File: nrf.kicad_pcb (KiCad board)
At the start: 2 copper layers, 24 parts, among them SW1 SW_DPST_x2, U1 BLYST-NRF52832-NANO, U2 Oled_128x64_SSD1306, U3 ECH8693R-TL-W, U4 C0720B001F, U5 MCP73871-xxI_ML, U6 LIS3DH

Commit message: More power setup
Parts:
- removed 100uF1, 10uF1: C_Small, Capacitors_SMD:C_0805
- added C4: 100nF, Capacitors_SMD:C_0805, F.Cu at (104.0, 73.0)
- added C5: 10uF, Capacitors_SMD:C_0805, F.Cu at (103.7, 78.2)
- added C6: 470pF, Capacitors_SMD:C_0805, F.Cu at (132.9, 96.0)
- added C7: 0.1uF, Capacitors_SMD:C_0805, F.Cu at (132.8, 100.2)
- added C8: 4.7uF, Capacitors_SMD:C_0805, F.Cu at (138.2, 97.7)
- added R11: 10K, Resistors_SMD:R_0805, F.Cu at (113.9, 61.2)
- added R12: 10K, Resistors_SMD:R_0805, F.Cu at (121.5, 61.4)
- added SW2: MID, my-fp-library:Tact_SW_3x6x3.5, F.Cu at (147.4, 59.8)
- added SW3: DWN, my-fp-library:Tact_SW_3x6x3.5, F.Cu at (157.6, 59.7)
- added U7: MIC5219-3.3BM5, TO_SOT_Packages_SMD:SOT-23-5, F.Cu at (138.3, 103.3)
- SW1: value SW_DPST_x2 -> UP; footprint Buttons_Switches_SMD:SW_DIP_x2_W5.08mm_Slide_Copal_CHS-A -> my-fp-library:Tact_SW_3x6x3.5
- moved SW1 37.8 mm to (137.2, 60.0)
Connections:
- net VBAT renamed /pwr/VBAT
- U1 pad 1: (no net) -> I2C_SDA
- U1 pad 11: (no net) -> /BTN_3
- U1 pad 13: (no net) -> /BTN_2
- U1 pad 2: (no net) -> I2C_SCL
- U6 pad 4: (no net) -> I2C_SCL
- U6 pad 6: (no net) -> I2C_SDA
- U6 pad 8: (no net) -> +3.3

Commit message: Connectors
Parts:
- added J1: Conn_01x02, my-fp-library:Battery Pads 3x3, F.Cu at (147.8, 112.7)
- added J2: Conn_01x05, Pin_Headers:Pin_Header_Straight_1x05_Pitch1.27mm, F.Cu at (142.7, 119.5)
- moved U1 35.1 mm to (117.0, 119.8), turned to 90 degrees
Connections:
- R1 pad 2: GND -> (GND)
- SW1 pad 1: GND -> (GND)
- SW2 pad 1: GND -> (GND)
- SW3 pad 1: GND -> (GND)
- U1 pad 18: (no net) -> /SWDIO
- U1 pad 19: (no net) -> /SWDCLK
- U1 pad 2: I2C_SCL -> /RESET
- U1 pad 3: (no net) -> I2C_SCL
- U2 pad 1: GND -> (GND)
- U2 pad 10: GND -> (GND)
- U2 pad 11: GND -> (GND)
- U2 pad 12: GND -> (GND)
- U2 pad 21: GND -> (GND)
- U2 pad 22: GND -> (GND)
- U2 pad 23: GND -> (GND)
- U2 pad 24: GND -> (GND)
- U2 pad 25: GND -> (GND)
- U2 pad 29: GND -> (GND)
- U2 pad 30: GND -> (GND)
- U2 pad 6: VDD -> +3.3
- U2 pad 8: GND -> (GND)
- U2 pad 9: VDD -> +3.3
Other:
- board outline added: 26.6 x 19.3 mm

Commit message: Layout power
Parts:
- moved R7 71.8 mm to (79.8, 77.0), turned to 180 degrees
- moved R6 70.4 mm to (79.8, 79.1)
- moved J1 70.4 mm to (77.7, 106.6)
- moved U5 68.0 mm to (84.2, 80.0)
- moved R4 67.7 mm to (75.2, 94.5)
- moved R8 67.2 mm to (88.8, 82.3)
- moved R10 65.6 mm to (79.8, 81.1), turned to 180 degrees
- moved R9 62.7 mm to (88.8, 80.2)
- moved R5 62.5 mm to (75.1, 89.9)
- moved D2 60.6 mm to (75.4, 87.8)
- moved C4 56.2 mm to (159.3, 82.8)
- moved R11 56.2 mm to (169.2, 70.9)
- moved R12 56.2 mm to (176.9, 71.1)
- moved U6 56.2 mm to (172.8, 83.3)
- moved C5 56.2 mm to (159.1, 87.9)
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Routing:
- net VBUS: track 0.00 -> 8.98 mm, vias 0 -> 3
- net Net-(C3-Pad1): track 0.00 -> 3.80 mm
- net Net-(R6-Pad2): track 0.00 -> 3.62 mm
- net Net-(R8-Pad1): track 0.00 -> 2.70 mm
- net (GND): track 0.00 -> 2.31 mm, vias 0 -> 6
- net Net-(R9-Pad1): track 0.00 -> 1.74 mm
- net Net-(R10-Pad1): track 0.00 -> 1.45 mm
- added copper zone on Gnd.Cu, net (GND)
- added copper zone on Pwr.Cu, net VBUS
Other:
- copper layers 2 -> 4

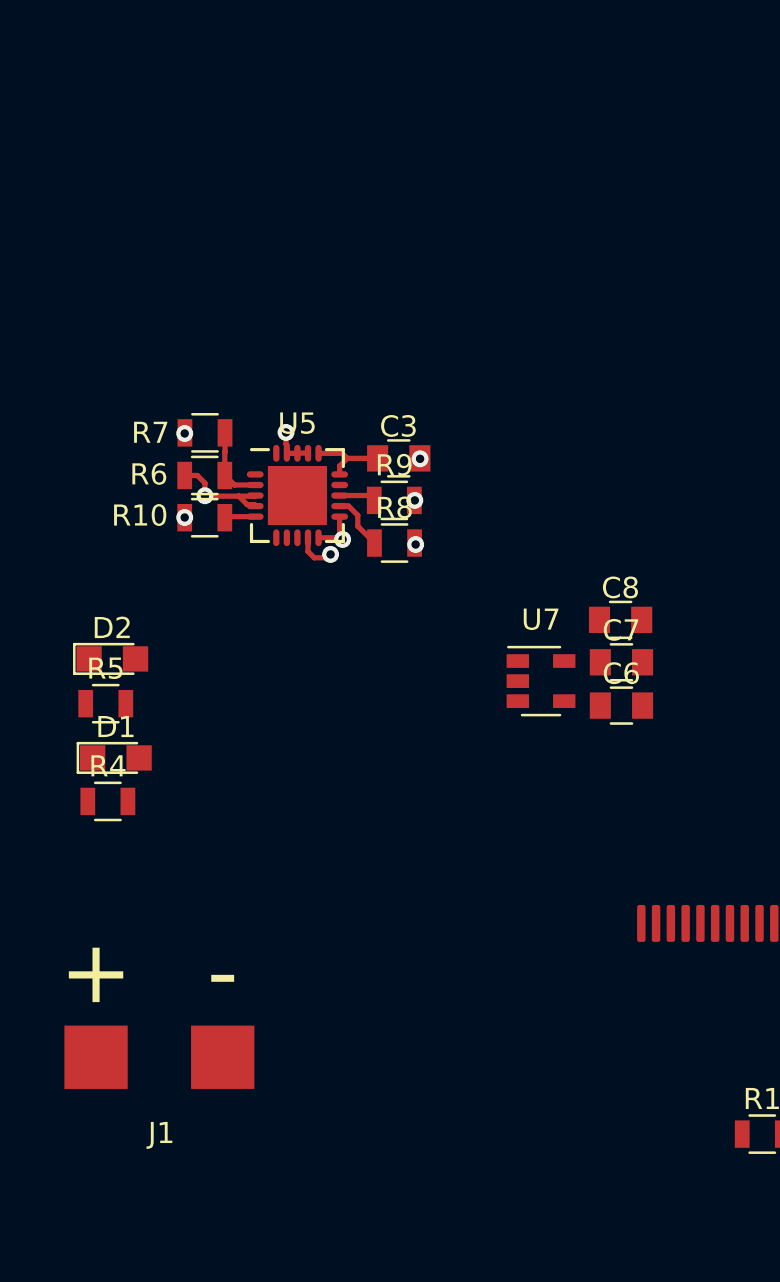
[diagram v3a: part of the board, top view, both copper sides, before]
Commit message: More power connections
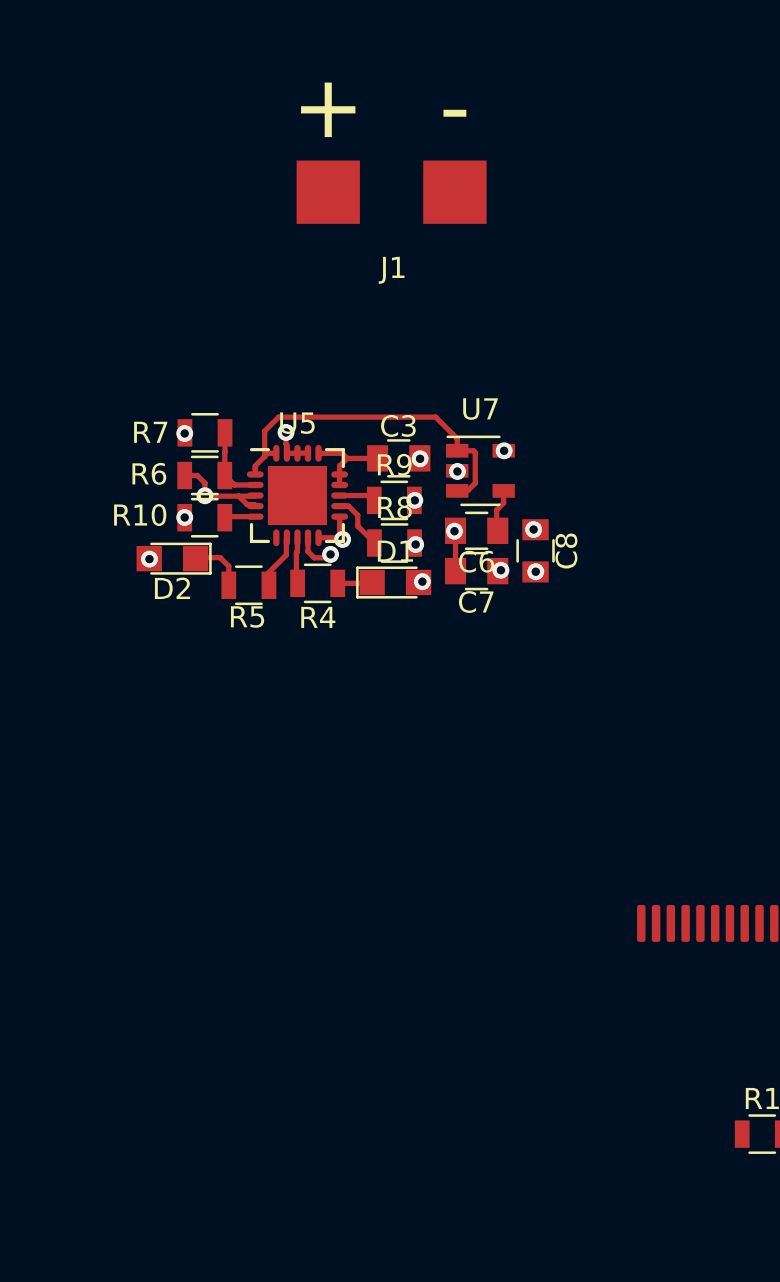
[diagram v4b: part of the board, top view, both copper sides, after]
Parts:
- moved J1 42.4 mm to (88.7, 65.6)
- moved D1 15.6 mm to (88.8, 84.1)
- moved R4 14.3 mm to (85.2, 84.2), turned to 180 degrees
- moved C6 10.8 mm to (92.7, 81.7), turned to 180 degrees
- moved U7 10.4 mm to (92.9, 78.8)
- moved R5 8.80 mm to (81.9, 84.3)
- moved C7 8.11 mm to (92.7, 83.6), turned to 180 degrees
- moved D2 5.54 mm to (78.3, 83.0), turned to 180 degrees
- moved C8 5.19 mm to (95.5, 82.6), turned to 270 degrees
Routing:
- net /pwr/VBAT: track 0.00 -> 16.6 mm
- net STAT: track 0.00 -> 2.61 mm
- net Net-(D2-Pad1): track 0.00 -> 2.60 mm
- net PWR_SENSE: track 0.00 -> 2.15 mm
- net Net-(C6-Pad1): track 0.00 -> 1.94 mm
- net (GND): track 2.31 -> 4.22 mm, vias 6 -> 9
- net Net-(D1-Pad1): track 0.00 -> 1.62 mm
- net VBUS: vias 3 -> 5
- net +3.3: vias 0 -> 3
- added copper zone on Pwr.Cu, net +3.3

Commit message: More PCB setup
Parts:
- Ue: renamed from U2; moved to B.Cu
- moved U1 88.3 mm to (81.3, 89.4)
- moved R12 77.5 mm to (100.1, 81.6)
- moved U6 72.4 mm to (100.6, 78.7)
- moved R11 66.1 mm to (103.5, 78.2), turned to 270 degrees
- moved C4 63.6 mm to (95.8, 78.8), turned to 90 degrees
- moved C5 61.9 mm to (97.6, 80.8), turned to 90 degrees
- moved J2 49.4 mm to (99.0, 96.5), turned to 90 degrees
- moved C1 39.7 mm to (89.5, 86.5)
- moved C2 39.0 mm to (88.6, 92.8)
- moved U4 27.9 mm to (99.1, 90.3), turned to 180 degrees
- moved Ue 21.4 mm to (91.9, 89.3)
- moved R1 19.2 mm to (100.8, 91.8)
- moved U3 13.0 mm to (103.8, 84.3)
- moved R3 12.0 mm to (103.8, 81.5)
- moved R2 9.02 mm to (100.3, 83.8)
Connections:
- R2 pad 1: GND -> (GND)
- U3 pad 1: GND -> (GND)
- U3 pad 3: GND -> (GND)
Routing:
- net +3.3: track 0.00 -> 13.7 mm, vias 3 -> 4
- net (GND): track 4.22 -> 12.2 mm, vias 9 -> 12
- net Net-(R3-Pad1): track 0.00 -> 3.37 mm
- net MOTOR_PWM: track 0.00 -> 2.46 mm
- net I2C_SCL: track 0.00 -> 1.64 mm
- net I2C_SDA: track 0.00 -> 1.60 mm
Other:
- net class Default: clearance 0.2 -> 0.1524; trace_width 0.25 -> 0.1524; via_dia 0.8 -> 0.6858; via_drill 0.4 -> 0.3302
- rule pad_to_mask_clearance: 0.051 -> 0.0508
- rule trace_clearance: 0.2 -> 0.1524
- rule trace_min: 0.2 -> 0.1524
- rule via_min_drill: 0.3 -> 0.254
- rule via_min_size: 0.4 -> 0.508

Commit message: Initial
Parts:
- removed J1: Conn_01x02, my-fp-library:Battery Pads 3x3
- removed U1: BLYST-NRF52832-NANO, my-fp-library:BLYST NRF52832-NANO
- removed U3: ECH8693R-TL-W, my-fp-library:SOT-28FL
- removed U4: C0720B001F, my-fp-library:VIBRATION MOTOR COIN 3V FLEX - C0720B001F
- removed U6: LIS3DH, my-fp-library:LGA-16_3x3mm
- removed Ue: Oled_128x64_SSD1306, my-fp-library:oled ssd1306 29x0.7mm
- added C10: 22pF, Capacitors_SMD:C_0603_HandSoldering, F.Cu at (148.4, 92.5)
- added C11: 1uF, Capacitors_SMD:C_0603_HandSoldering, F.Cu at (125.2, 97.9)
- added C12: 10uF, Capacitors_SMD:C_0603_HandSoldering, F.Cu at (129.8, 97.9)
- added C9: 10uF, Capacitors_SMD:C_0603_HandSoldering, F.Cu at (146.7, 110.5)
- added D4: ZLLS410, Diodes_SMD:D_SOD-323, F.Cu at (134.3, 98.2)
- added IC1: BMA423, SamacSys_Parts:BMA423, F.Cu at (173.6, 80.6)
- added IC2: 113990582, SamacSys_Parts:113990582, F.Cu at (126.2, 84.7)
- added J4: Conn_01x06, Pin_Headers:Pin_Header_Straight_1x06_Pitch2.54mm, F.Cu at (168.9, 80.2)
- added J6: CONN_01X05, Pin_Headers:Pin_Header_Straight_1x05_Pitch2.54mm, F.Cu at (125.0, 106.3)
- added P1: BATT, my-fp-library:Battery Pads 3x3, F.Cu at (132.1, 106.1)
- added Q1: SI3139K, TO_SOT_Packages_SMD:SOT-23, F.Cu at (140.8, 64.0)
- added Q2: MGSF1N02L, TO_SOT_Packages_SMD:SOT-23, F.Cu at (157.7, 78.1)
- added Q3: SI3139K, TO_SOT_Packages_SMD:SOT-23, F.Cu at (124.0, 63.2)
- added Q4: SI3139K, TO_SOT_Packages_SMD:SOT-23, F.Cu at (111.7, 62.7)
- added R13: 100, Resistors_SMD:R_0603_HandSoldering, F.Cu at (116.3, 59.6)
- added R14: 100K, Resistors_SMD:R_0603_HandSoldering, F.Cu at (135.7, 114.7)
- added R15: 1K, Resistors_SMD:R_0603_HandSoldering, F.Cu at (146.2, 105.6)
- added R16: 10K, Resistors_SMD:R_0603_HandSoldering, F.Cu at (141.5, 111.8)
- added R17: 10K, Resistors_SMD:R_0603_HandSoldering, F.Cu at (148.1, 95.1)
- added R18: 10K, Resistors_SMD:R_0603_HandSoldering, F.Cu at (155.6, 98.0)
- added R19: 10K, Resistors_SMD:R_0603_HandSoldering, F.Cu at (156.4, 93.2)
- added SW4: DWN, my-fp-library:Tact_SW_3x6x3.5, F.Cu at (141.2, 88.8)
- added U2: C0720B001F, my-fp-library:VIBRATION MOTOR COIN 3V FLEX - C0720B001F, F.Cu at (144.5, 82.1)
- C1: value C -> 22pF; footprint Capacitors_SMD:C_0805 -> Capacitors_SMD:C_0603_HandSoldering
- C2: value C -> 1uF; footprint Capacitors_SMD:C_0805 -> Capacitors_SMD:C_0603_HandSoldering
- C3: value 10uF -> 470pF; footprint Capacitors_SMD:C_0805 -> Capacitors_SMD:C_0603_HandSoldering
- C4, C6: footprint Capacitors_SMD:C_0805 -> Capacitors_SMD:C_0603_HandSoldering
- C5: value 10uF -> 100nF; footprint Capacitors_SMD:C_0805 -> Capacitors_SMD:C_0603_HandSoldering
- C7: value 0.1uF -> 470pF; footprint Capacitors_SMD:C_0805 -> Capacitors_SMD:C_0603_HandSoldering
- C8: value 4.7uF -> 0.1uF; footprint Capacitors_SMD:C_0805 -> Capacitors_SMD:C_0603_HandSoldering
- R1: value R -> 330; footprint Resistors_SMD:R_0805 -> Resistors_SMD:R_0603_HandSoldering
- R10: value 10K -> 30; footprint Resistors_SMD:R_0805 -> Resistors_SMD:R_0603_HandSoldering
- R11, R12, R4, R5, R6, R7, R8: footprint Resistors_SMD:R_0805 -> Resistors_SMD:R_0603_HandSoldering
- R2: value 10K -> 100K; footprint Resistors_SMD:R_0805 -> Resistors_SMD:R_0603_HandSoldering
- R3: value 330 -> 2.2K; footprint Resistors_SMD:R_0805 -> Resistors_SMD:R_0603_HandSoldering
- R9: value 1K -> 100K; footprint Resistors_SMD:R_0805 -> Resistors_SMD:R_0603_HandSoldering
- SW3: value DWN -> BACK
- U5: value MCP73871-xxI_ML -> MIC5219-3.3YM5; footprint Housings_DFN_QFN:UQFN-20-1EP_4x4mm_Pitch0.5mm -> TO_SOT_Packages_SMD:SOT-23-5
- U7: value MIC5219-3.3BM5 -> MCP73871-xxI_ML; footprint TO_SOT_Packages_SMD:SOT-23-5 -> Housings_DFN_QFN:QFN-20-1EP_4x4mm_Pitch0.5mm
- moved C5 85.6 mm to (183.1, 79.3), turned to 0 degrees
- moved C4 82.7 mm to (178.5, 79.3), turned to 0 degrees
- moved R11 79.0 mm to (182.4, 81.9), turned to 0 degrees
- moved R12 78.1 mm to (178.2, 81.9)
- moved R8 69.4 mm to (157.7, 90.4)
- moved U5 67.0 mm to (141.0, 115.6)
- moved D2 66.7 mm to (135.3, 117.5), turned to 0 degrees
- moved R9 65.1 mm to (151.5, 98.0)
- moved R6 64.8 mm to (135.7, 111.8)
- moved C3 64.1 mm to (145.7, 108.2)
- moved J2 63.6 mm to (160.3, 79.5), turned to 0 degrees
- moved C2 62.9 mm to (150.9, 84.4)
- moved C6 62.8 mm to (145.8, 115.2), turned to 0 degrees
- moved C7 61.4 mm to (146.7, 112.9), turned to 0 degrees
- moved C8 60.1 mm to (155.6, 84.4), turned to 0 degrees
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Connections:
- C1 pad 1: Net-(C1-Pad1) -> /XL1
- C1 pad 2: Net-(C1-Pad2) -> (GND)
- C2 pad 1: Net-(C2-Pad1) -> +3.3
- C2 pad 2: Net-(C2-Pad2) -> (GND)
- C6 pad 1: Net-(C6-Pad1) -> +3.3V
- C7 pad 1: +3.3 -> +3.3V
- R1 pad 1: Net-(R1-Pad1) -> /MOTOR_PWM
- R1 pad 2: (GND) -> Net-(Q2-Pad1)
- R10 pad 1: Net-(R10-Pad1) -> /LEDK
- R10 pad 2: (GND) -> Net-(Q3-Pad3)
- R2 pad 1: (GND) -> +3.3
- R2 pad 2: MOTOR_PWM -> /LIGHT3
- R3 pad 1: Net-(R3-Pad1) -> /LEDK
- R8 pad 1: Net-(R8-Pad1) -> +3.3
- R8 pad 2: (GND) -> /LIGHT1
- R9 pad 1: Net-(R9-Pad1) -> +3.3
- R9 pad 2: (GND) -> /LIGHT2
- U5 pad 1: /pwr/VBAT -> +5
- U5 pad 2: Net-(R6-Pad2) -> (GND)
- U5 pad 3: VBUS -> +5
- U5 pad 4: VBUS -> Net-(C3-Pad1)
- U5 pad 5: Net-(R10-Pad1) -> +3.3V
- U7 pad 1: /pwr/VBAT -> +5
- U7 pad 2: (GND) -> Net-(R6-Pad2)
- U7 pad 3: /pwr/VBAT -> VBUS
- U7 pad 4: Net-(C6-Pad1) -> VBUS
- U7 pad 5: +3.3 -> Net-(R16-Pad1)
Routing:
- net /pwr/VBAT: track 16.6 -> 0.00 mm
- net +3.3: track 13.7 -> 0.00 mm, vias 4 -> 0
- net (GND): track 12.2 -> 0.00 mm, vias 12 -> 0
- net VBUS: track 8.98 -> 0.00 mm, vias 5 -> 0
- net Net-(C3-Pad1): track 4.28 -> 0.00 mm
- net Net-(R6-Pad2): track 3.62 -> 0.00 mm
- net Net-(R3-Pad1): track 3.37 -> 0.00 mm
- net Net-(R8-Pad1): track 2.70 -> 0.00 mm
- net STAT: track 2.61 -> 0.00 mm
- net Net-(D2-Pad1): track 2.60 -> 0.00 mm
- net MOTOR_PWM: track 2.46 -> 0.00 mm
- net PWR_SENSE: track 2.15 -> 0.00 mm
- net Net-(C6-Pad1): track 1.94 -> 0.00 mm
- net Net-(R9-Pad1): track 1.74 -> 0.00 mm
- net I2C_SCL: track 1.64 -> 0.00 mm
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- removed copper zone on Gnd.Cu, net (GND)
- removed copper zone on Pwr.Cu, net +3.3
- removed copper zone on Pwr.Cu, net VBUS
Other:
- board outline removed

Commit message: Update for accel
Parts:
- removed J4: Conn_01x06, Pin_Headers:Pin_Header_Straight_1x06_Pitch2.54mm
- added J7: Conn_01x12, my-fp-library:FPC_12x0.7mm, F.Cu at (153.8, 70.2)
- C4, C5: value 100nF -> 0.1uF
- moved R11 20.0 mm to (168.8, 96.6)
- moved C5 19.7 mm to (173.6, 96.5)
- moved C4 14.9 mm to (173.8, 93.4)
- moved IC1 12.6 mm to (168.9, 92.3)
- moved R12 10.0 mm to (173.9, 91.0)
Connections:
- IC1 pad 12: I2C_SCL -> /SCL
- IC1 pad 2: I2C_SDA -> /SDA
- IC1 pad 5: XL_INT_1 -> (no net)
- IC1 pad 6: XL_INT_2 -> (no net)
- IC2 pad 27: (no net) -> /SCL
- IC2 pad 29: (no net) -> /SDA
- IC2 pad 36: (no net) -> /SPI_SCK
- IC2 pad 37: (no net) -> /SPI_MOSI
- IC2 pad 38: (no net) -> /SPI_CS
- IC2 pad 39: (no net) -> /SPI_DC
- IC2 pad 47: (no net) -> /SPI_RESET
- R11 pad 2: I2C_SCL -> /SDA
- R12 pad 2: I2C_SDA -> /SCL
- R18 pad 1: (no net) -> /SPI_RESET
- R19 pad 1: (no net) -> /SPI_CS

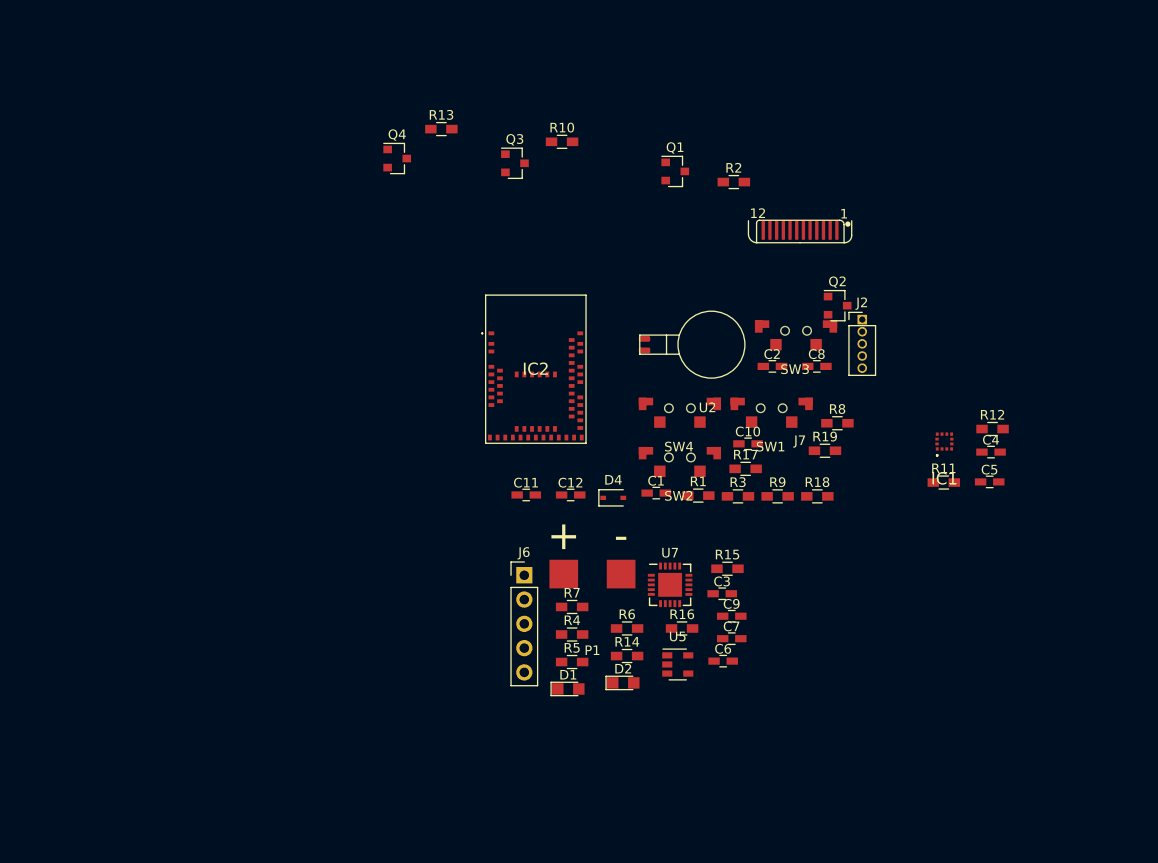
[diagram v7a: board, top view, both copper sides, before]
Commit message: Move power from sub sheet
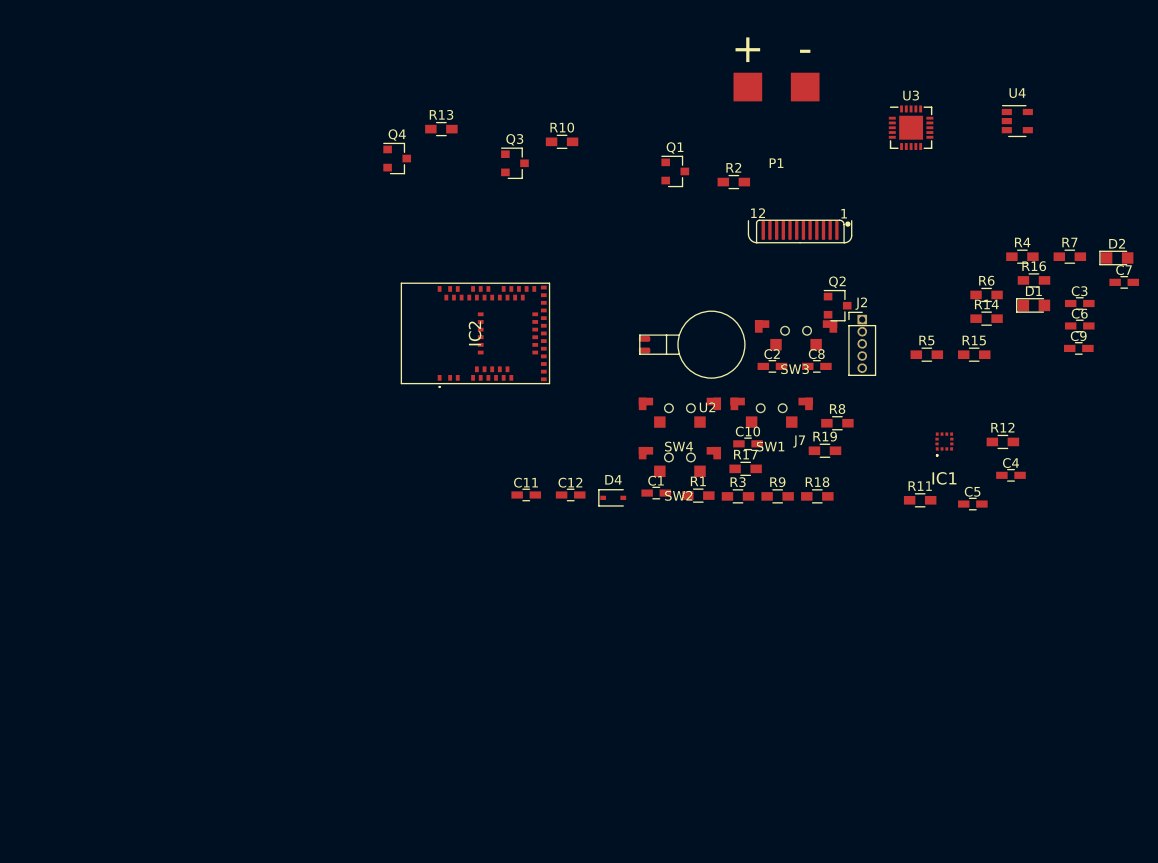
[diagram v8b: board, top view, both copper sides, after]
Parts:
- removed J6: CONN_01X05, Pin_Headers:Pin_Header_Straight_1x05_Pitch2.54mm
- removed U5: MIC5219-3.3YM5, TO_SOT_Packages_SMD:SOT-23-5
- removed U7: MCP73871-xxI_ML, Housings_DFN_QFN:QFN-20-1EP_4x4mm_Pitch0.5mm
- added U3: MCP73871-xxI_ML, Housings_DFN_QFN:QFN-20-1EP_4x4mm_Pitch0.5mm, F.Cu at (165.4, 59.4)
- added U4: MIC5219-3.3YM5, TO_SOT_Packages_SMD:SOT-23-5, F.Cu at (176.5, 58.7)
- C3: value 470pF -> 10uF
- C9: value 10uF -> 470pF
- moved D2 68.2 mm to (187.0, 73.1)
- moved R7 63.7 mm to (182.0, 72.9)
- moved D1 63.1 mm to (178.3, 78.0)
- moved R4 61.5 mm to (177.1, 72.9)
- moved C7 55.4 mm to (187.7, 75.6)
- moved P1 54.5 mm to (151.3, 55.2)
- moved R16 51.8 mm to (178.3, 75.4)
- moved R14 51.6 mm to (173.3, 79.4)
- moved R6 51.3 mm to (173.3, 76.9)
- moved C6 51.2 mm to (183.1, 80.2)
- moved R5 49.1 mm to (167.1, 83.2)
- moved C3 48.2 mm to (183.1, 77.8)
- moved C9 45.9 mm to (183.0, 82.5)
- moved R15 34.2 mm to (172.0, 83.2)
- moved IC2 7.34 mm to (119.9, 81.0), turned to 90 degrees
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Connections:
- C6 pad 1: +3.3V -> Net-(C6-Pad1)
- C7 pad 1: +3.3V -> +3.3
- C9 pad 1: Net-(C9-Pad1) -> +3.3
- D1 pad 2: VBUS -> +5
- D2 pad 2: VBUS -> +5
- IC2 pad 56: (no net) -> /PWR_SENSE
- IC2 pad 57: (no net) -> /PWR_STAT
- P1 pad 1: Net-(C9-Pad1) -> Net-(C3-Pad1)
- R4 pad 2: PWR_SENSE -> /PWR_SENSE
- R5 pad 2: STAT -> /PWR_STAT
- R6 pad 1: VBUS -> +5
